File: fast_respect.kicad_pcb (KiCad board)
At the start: 2 copper layers, 70 x 110 mm, 97 parts, among them J1_1 Conn_02x04_Odd_Even, J5_1 Conn_02x03_Odd_Even, J5_2 Conn_02x03_Odd_Even, J7_1 Conn_01x02, Q2_1 AONM7421, Q3_1 IRLML6344T, Q4_1 IRLML6344T, Q4_2 IRLML6344T, Q4_3 IRLML6344T, Q4_4 IRLML6344T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

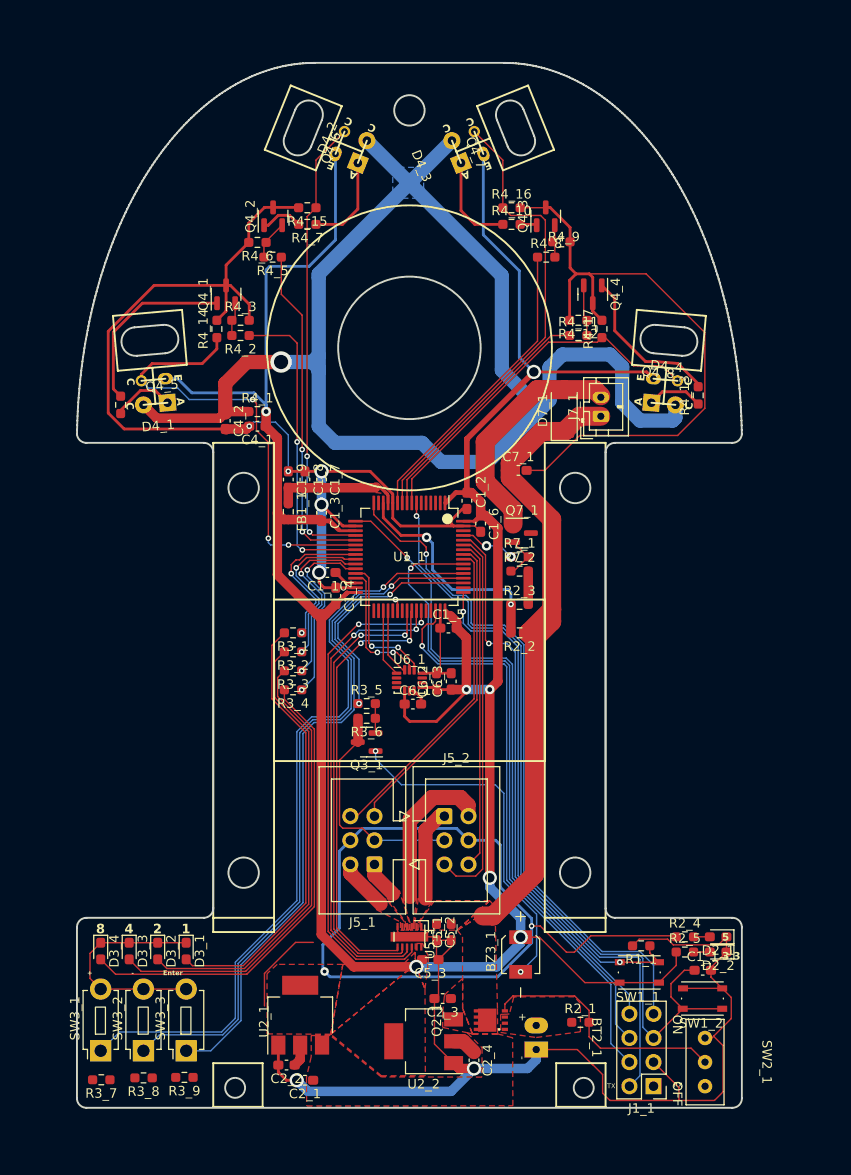
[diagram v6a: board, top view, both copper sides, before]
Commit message: 全て配線して電気的なDRCは消した
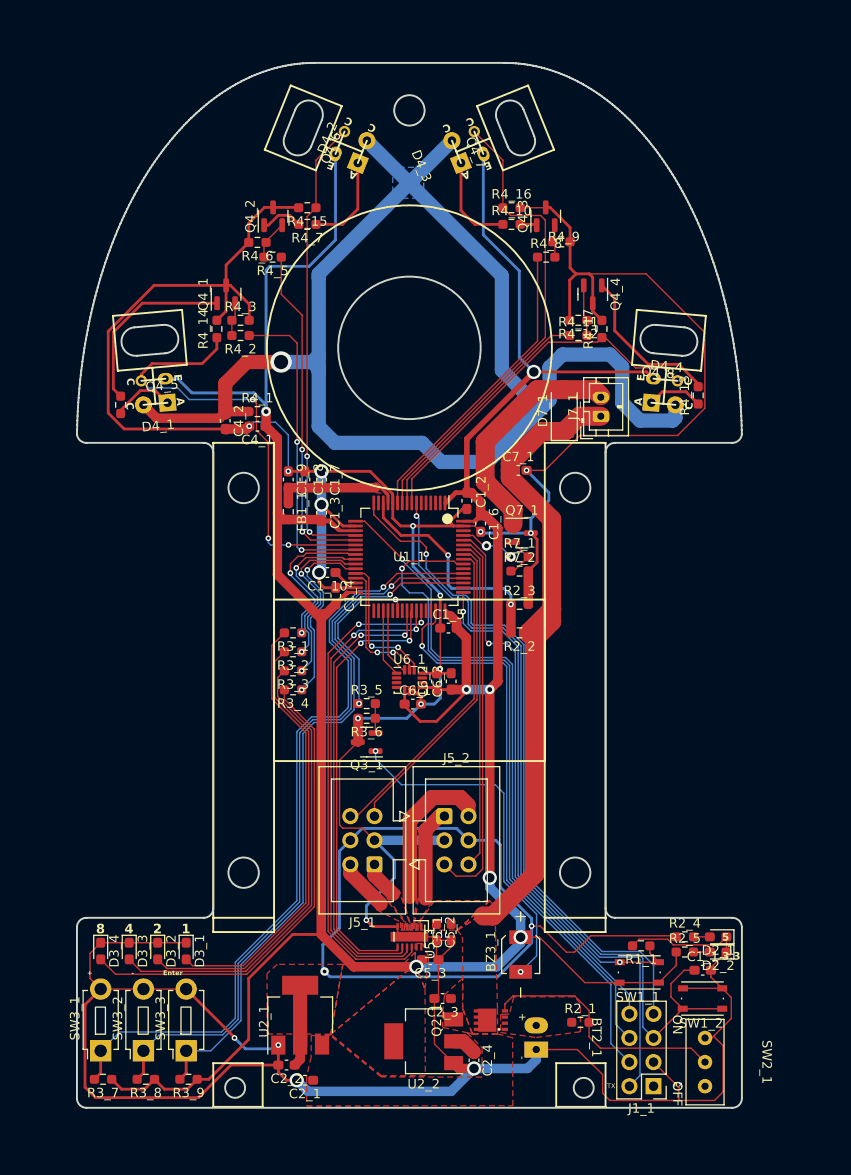
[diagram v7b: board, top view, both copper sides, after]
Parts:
- moved R3_9 0.48 mm to (-58.2, 107.0)
- moved R3_8 0.28 mm to (-62.8, 107.0)
- moved R3_7 0.19 mm to (-67.2, 107.0)
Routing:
- net GND: track 372.3 -> 473.2 mm, vias 7 -> 18
- net +3.3V: track 310.5 -> 333.8 mm
- net +5V: track 86.8 -> 93.1 mm
- net UI_SW_3: track 71.7 -> 75.0 mm
- net UI_SW_2: track 76.4 -> 79.6 mm
- net UI_SW_1: track 81.1 -> 84.4 mm
- net SWO: track 69.0 -> 71.2 mm

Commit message: ベタ塗った（ビアない段階だがきれい）
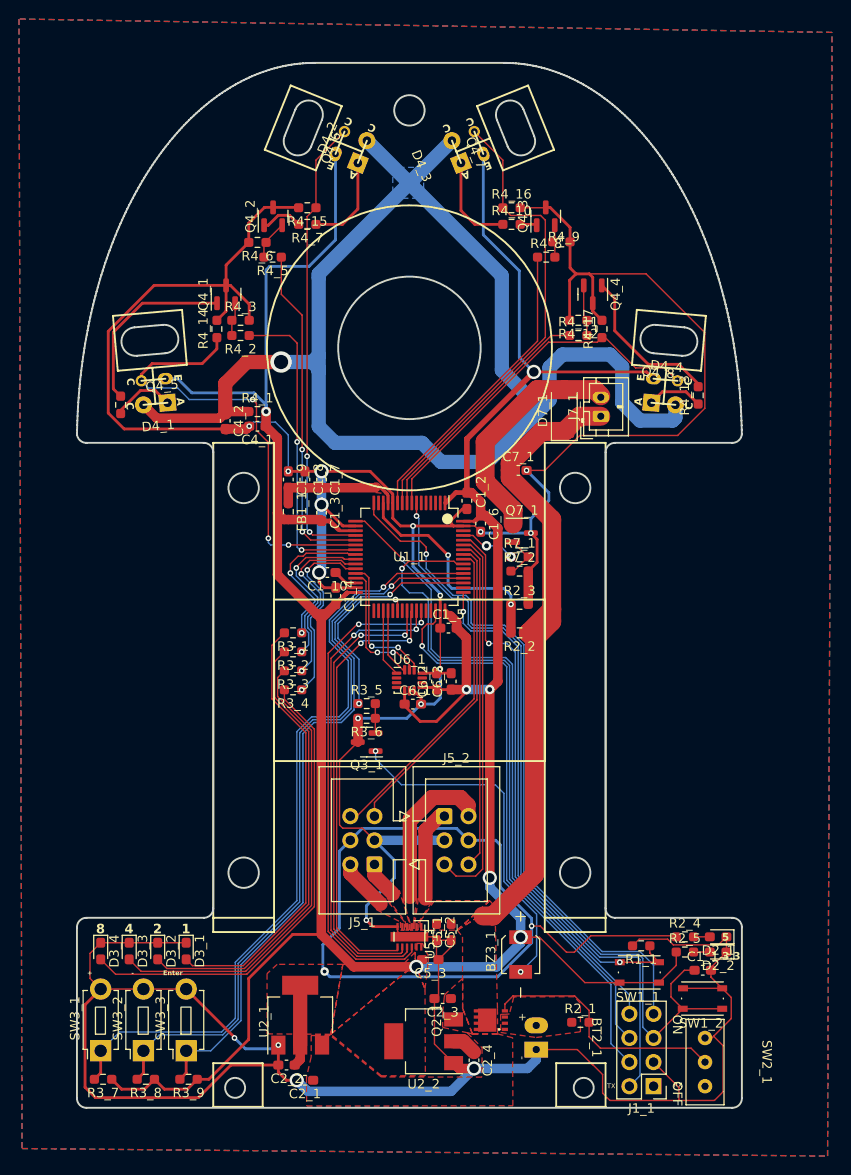
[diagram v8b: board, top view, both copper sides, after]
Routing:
- added copper zone on B.Cu, net GND
- added copper zone on F.Cu, net GND
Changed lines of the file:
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@@
+    )
+  )
+  (zone (net 6) (net_name "GND") (layers "F&B.Cu") (hatch edge 0.5)
+    (priority 1)
+    (connect_pads yes (clearance 0.5))
+    (min_thickness 0.25) (filled_areas_thickness no)
+    (fill yes (thermal_gap 0.5) (thermal_bridge_width 0.5) (island_removal_mode 1) (island_area_min 10))
+    (polygon
+      (pts
+        (xy -76.1 -4.62)
+        (xy -75.78 114.29)
+        (xy 9.02 115.08)
+        (xy 9.49 -3.21)
+      )
     )
   )
